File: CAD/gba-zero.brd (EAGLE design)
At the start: 130.7 x 72.9 mm, 55 parts, among them IC5 APX803, Q2 BSS138, U1 NC7WZ16, U4 LM4875

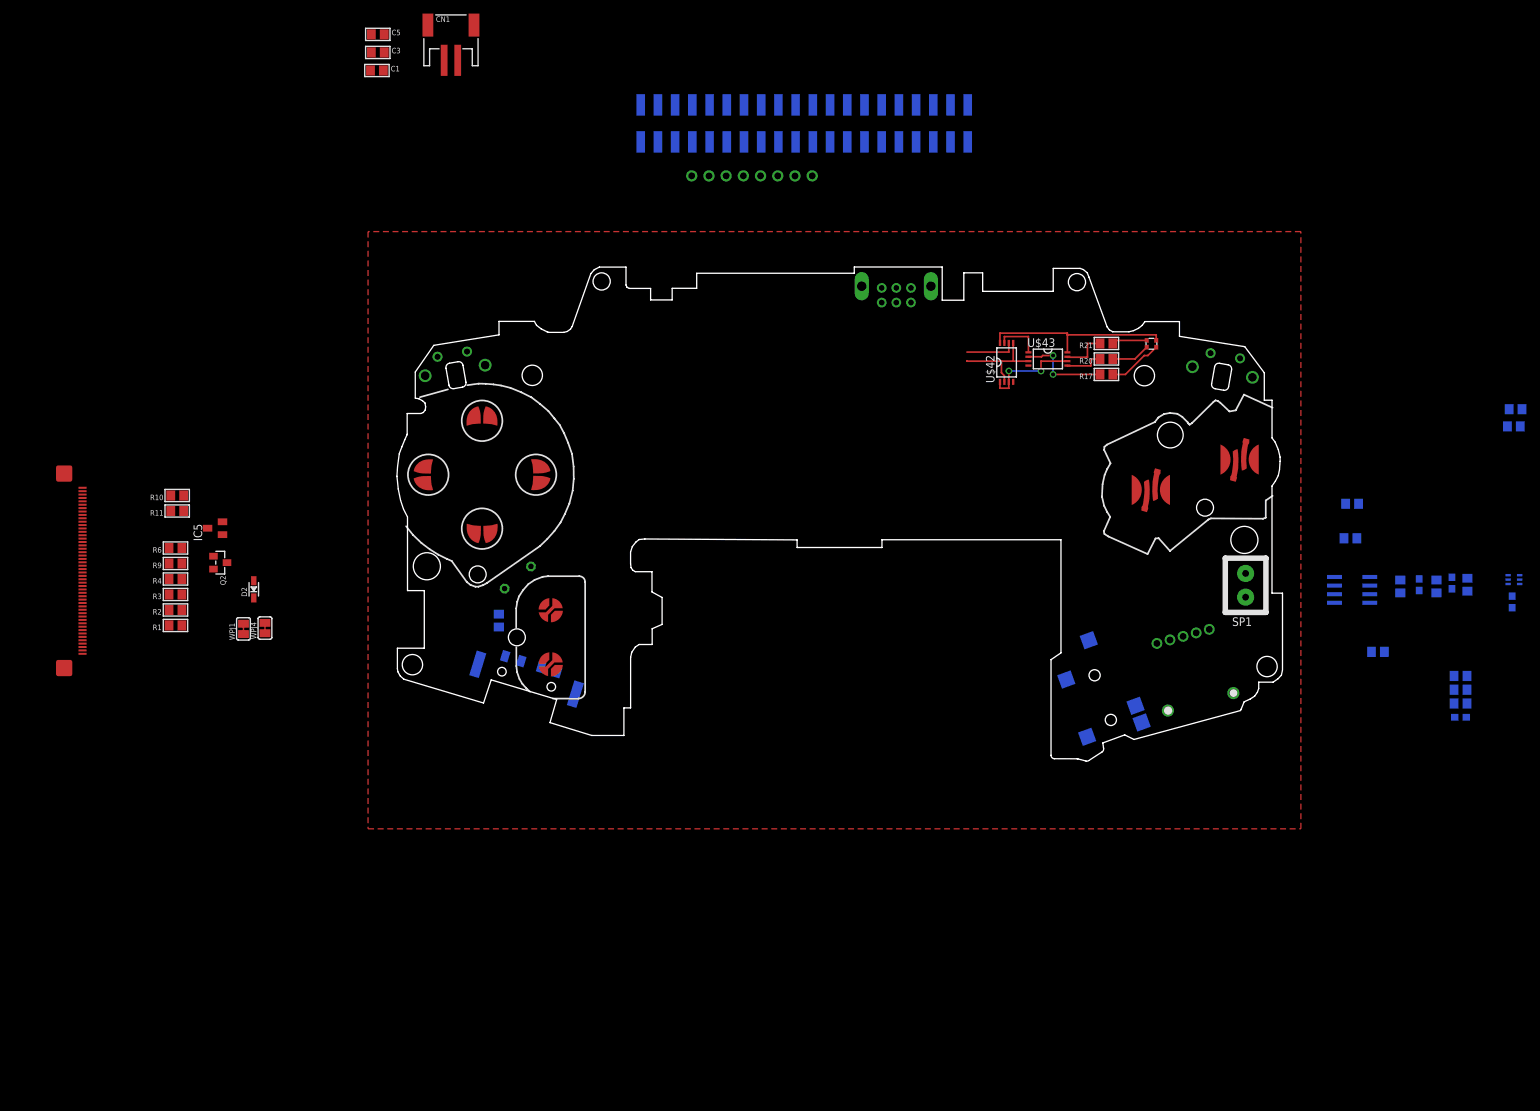
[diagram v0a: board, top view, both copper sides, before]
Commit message: Routed right side of the board
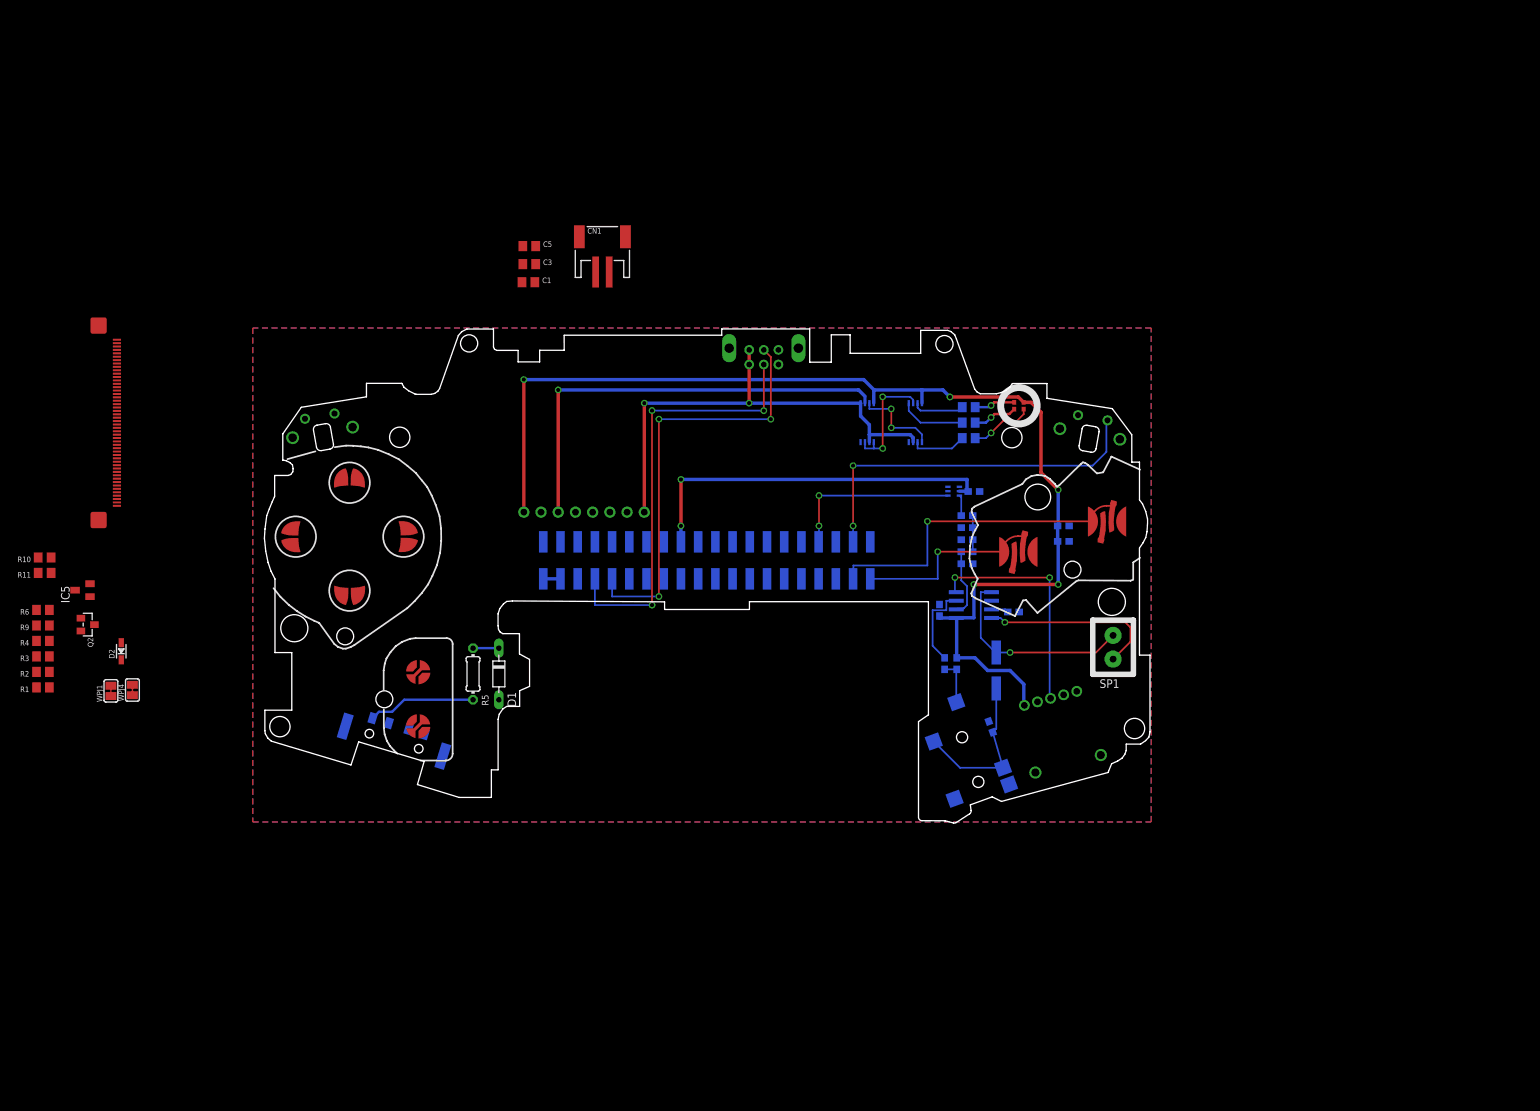
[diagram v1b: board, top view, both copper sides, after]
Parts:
- removed C15, C18: 10u, rcl:C0805
- removed C17: 100n, rcl:C0805
- removed C4: 100μF, rcl:C0603
- removed C8: 0.1μF, rcl:C0603
- removed R22, R23: 100K, microbuilder:0805
- removed U4: LM4875, texas:SOIC8
- added C10: 47μF, microbuilder:0603
- added C11: 10μF, microbuilder:0603
- added C7, C9: 0.1μF, microbuilder:0603
- added R13, R14: 100K, microbuilder:0603
- added U2: LM4875, gba-zero-parts:SO-8
- C12: value 10u -> 10μF; device rcl:C0805 -> microbuilder:0603
- C13: value 10u -> 100uF; device rcl:C0805 -> microbuilder:PANASONIC_D
- C2: value 0.1μF -> 1.0μF; device rcl:C0603 -> microbuilder:0603
- C6: value 47μF -> 1.0μF; device rcl:C0603 -> microbuilder:0603
- D1: device diode:D-5 -> diode:D-7.5
- R12, R24, R7, R8: device microbuilder:0805 -> microbuilder:0603
- R5: device microbuilder:0805 -> resistor:0204/7
- moved U1 83.7 mm to (103.4, 48.8), turned to 180 degrees
- moved R7 74.6 mm to (105.4, 45.2), turned to 0 degrees
- moved C6 70.9 mm to (101.3, 31.2)
- moved R8 69.6 mm to (105.4, 41.7), turned to 0 degrees
- moved R24 69.4 mm to (108.9, 14.0), turned to 250 degrees
- moved U$7 66.1 mm to (67.0, 38.6)
- moved C2 64.8 mm to (112.3, 31.0), turned to 180 degrees
- moved R12 64.0 mm to (105.4, 38.1), turned to 180 degrees
- moved C13 58.0 mm to (109.7, 22.4), turned to 90 degrees
- moved U$12 55.5 mm to (70.6, 44.5)
- moved C12 49.2 mm to (119.6, 41.4)
- moved C1 38.4 mm to (40.7, 79.7)
- moved C3 38.4 mm to (40.8, 82.3)
- moved CN1 38.4 mm to (51.6, 84.9)
- moved C5 38.4 mm to (40.8, 85.0)
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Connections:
- net N$19 renamed BAT
- removed net N$23: R22.1, U4.3
- removed net N$26: U$17.2, U4.4
- removed net N$30: C6.1, R12.1, U4.2
- removed net N$35: C12.1, U4.7
- removed net N$36: C4.1, SP1.1, U4.5
- removed net N$37: SP1.2, U4.8
- new net BYPASS: C2.1, U2.7
- new net IN-: C10.2, R12.1, U2.2
- new net SENSE: R14.2, U2.3
- new net VO1: C13.+, SP1.1, U2.5
- new net VO2: SP1.2, U2.8
- new net VOL/SD: U$17.2, U2.4
- net +5V: now also C11.2, C12.2, C6.2, R13.1, U2.1; no longer C13.2, C15.1, C17.1, C18.1, R23.1, U4.1
- net 3.3V: now also C7.1; no longer C8.2
- net BTN_A: now also U$7.38; no longer U$7.16
- net BTN_B: now also U$7.40; no longer U$7.32
- net BTN_D: now also U$7.15; no longer U$7.31
- net BTN_LS: now also L.SW; no longer L.BIG-1, L.SMALL-1
- net BTN_R: now also U$7.27; no longer U$7.15
- net BTN_RS: now also R.SW, U$7.37; no longer R.BIG-1, R.SMALL-1, U$7.11
- net BTN_SEL: now also U$7.32; no longer U$7.35
- net BTN_STR: now also U$7.28; no longer U$7.37
- net BTN_U: now also U$7.11; no longer U$7.29
- net GND: now also C11.1, C12.1, C2.2, C6.1, C7.2, C9.2, L.GND@1, L.GND@2, L.GND@3, R.GND@1, R.GND@2, R.GND@3, U2.6; no longer C12.2, C13.1, C15.2, C17.2, C18.2, C2.1, C8.1, L.BIG-2, L.SMALL-2, R.BIG-2, R.SMALL-2, U4.6
- net N$21: now also C10.1, C9.1; no longer C2.2, C6.2
- net N$22: now also R13.2, R14.1; no longer R22.2, R23.2
- net PWR_EN_RPI: now also U$7.16; no longer U$7.40
- net PWR_SW_SEN: now also U$7.26; no longer U$7.38
- net RING: now also C13.-; no longer C4.2
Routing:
- net +5V: track 28.2 -> 175.4 mm, vias 0 -> 5
- net TXD: track 0.00 -> 64.3 mm, vias 0 -> 3
- net RXD: track 0.00 -> 62.8 mm, vias 0 -> 3
- net LBO: track 7.52 -> 64.7 mm, vias 0 -> 1
- net 3.3V: track 0.00 -> 54.7 mm, vias 0 -> 2
- net USB: track 15.1 -> 69.5 mm, vias 0 -> 2
- net BTN_RS: track 0.00 -> 54.2 mm, vias 0 -> 2
- net BTN_A: track 0.00 -> 47.8 mm, vias 0 -> 1
- net VOL/SD: track 0.00 -> 34.2 mm, vias 0 -> 2
- net VO1: track 0.00 -> 29.8 mm, vias 0 -> 1
- net BTN_B: track 0.00 -> 27.7 mm, vias 0 -> 1
- net VO2: track 0.00 -> 26.8 mm, vias 0 -> 1
- net AUD_PWM: track 0.00 -> 25.9 mm, vias 0 -> 2
- net RING: track 0.00 -> 24.0 mm
- net N$17: track 0.00 -> 15.9 mm
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- added copper zone on layer 16, net GND

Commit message: More Routing
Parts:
- added C14, C4: 10μF, microbuilder:0603
- added C8: 0.1μF, microbuilder:0603
- moved R9 123.8 mm to (75.7, -33.7)
- moved U$2 117.3 mm to (62.1, -22.1)
- moved R6 117.1 mm to (70.3, -27.5), turned to 0 degrees
- moved Q2 116.6 mm to (75.7, -30.9), turned to 90 degrees
- moved R10 115.9 mm to (71.1, -16.3)
- moved R4 115.9 mm to (70.4, -29.4)
- moved R11 115.8 mm to (71.1, -18.4)
- moved R3 115.7 mm to (70.4, -31.5)
- moved R2 115.6 mm to (70.4, -33.5)
- moved R1 115.5 mm to (70.4, -35.5)
- moved IC5 110.9 mm to (70.1, -22.8), turned to 270 degrees
- moved D2 108.2 mm to (75.5, -26.7), turned to 270 degrees
- moved WPJ1 105.5 mm to (76.2, -21.9), turned to 180 degrees
- moved WPJ4 101.0 mm to (76.0, -18.0), turned to 180 degrees
- moved C1 56.6 mm to (-12.7, 60.9)
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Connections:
- net +5V: now also C14.1
- net 3.3V: now also C4.1, C8.1
- net GND: now also C14.2, C4.2, C8.2
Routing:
- net BTN_R: track 0.00 -> 80.8 mm, vias 0 -> 3
- net BTN_L: track 0.00 -> 77.3 mm, vias 0 -> 3
- net BTN_D: track 0.00 -> 75.4 mm, vias 0 -> 3
- net BTN_U: track 0.00 -> 67.3 mm, vias 0 -> 3
- net BTN_LS: track 0.00 -> 58.7 mm, vias 0 -> 2
- net 3.3V: track 54.7 -> 83.2 mm
- net N$1: track 0.00 -> 16.0 mm
- net TFT_RST: track 0.00 -> 9.49 mm
- net +5V: track 175.4 -> 184.4 mm
- net N$9: track 0.00 -> 8.50 mm
- net N$6: track 0.00 -> 7.55 mm
- net N$7: track 0.00 -> 6.23 mm
- net N$2: track 0.00 -> 5.86 mm
- net MOSI: track 0.00 -> 5.61 mm
- net SCLK: track 0.00 -> 5.41 mm
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
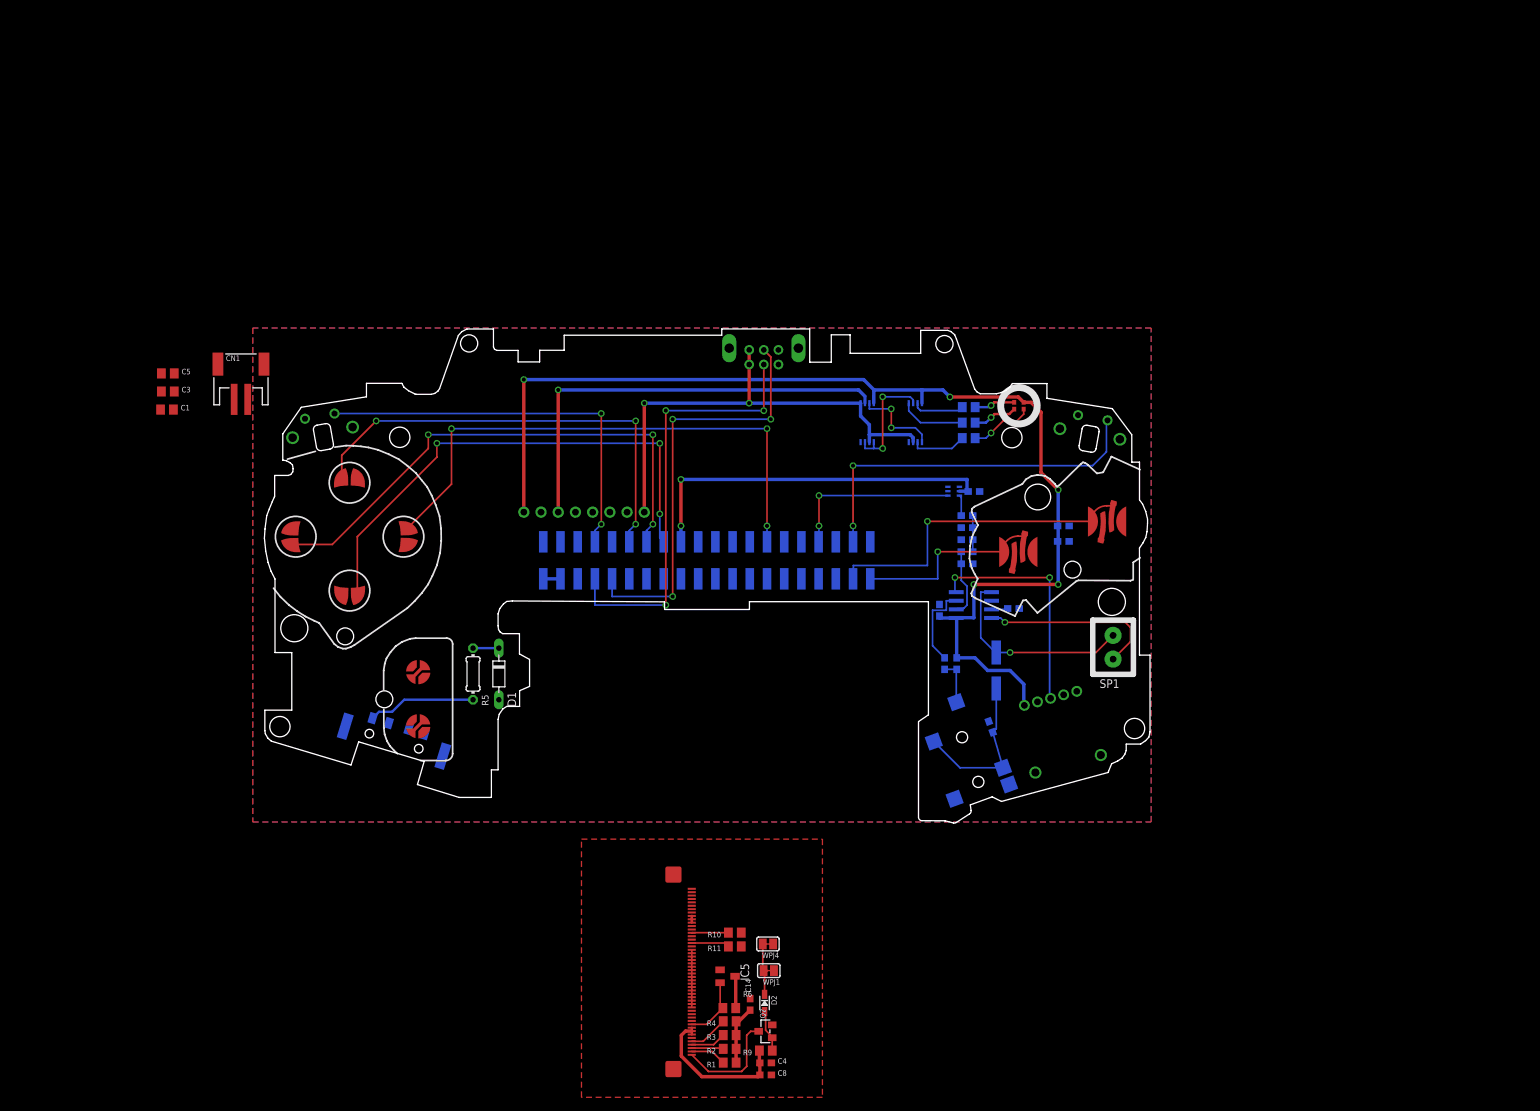
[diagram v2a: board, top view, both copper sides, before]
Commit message: Display is routed, some other stuff was unrouted
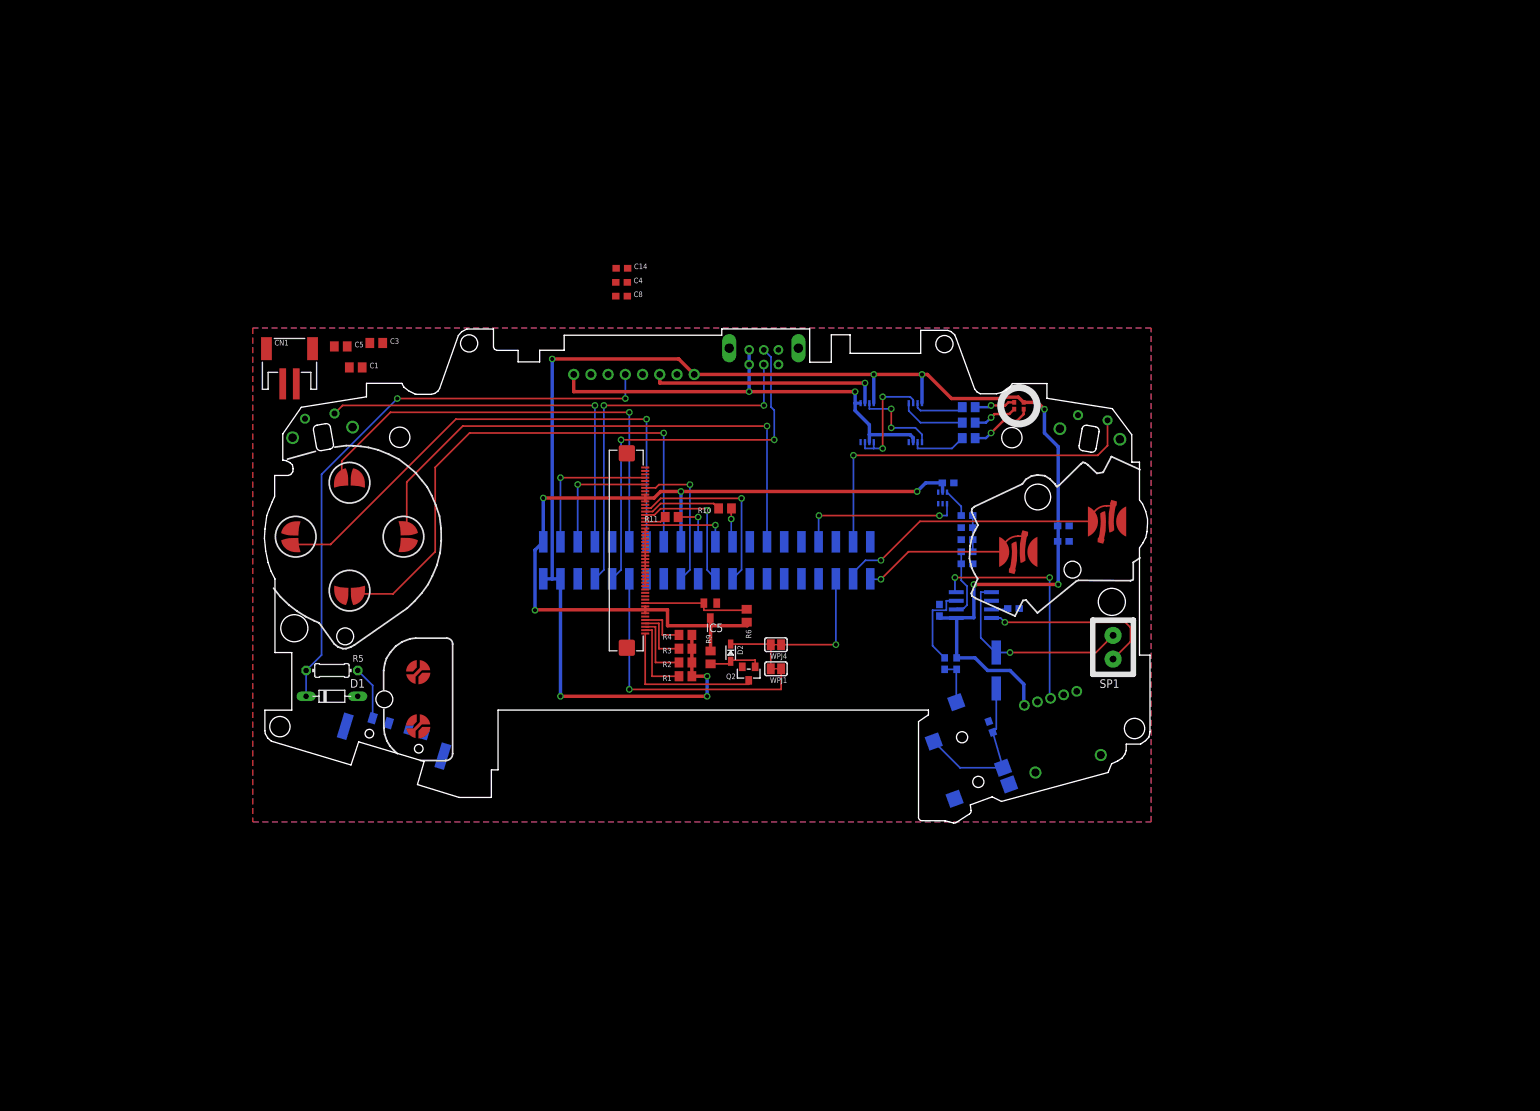
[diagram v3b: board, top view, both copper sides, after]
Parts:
- moved C4 117.1 mm to (54.4, 79.6)
- moved C8 116.9 mm to (54.4, 77.6)
- moved C14 110.3 mm to (54.5, 81.7), turned to 0 degrees
- moved R11 64.1 mm to (61.8, 45.0)
- moved R10 62.6 mm to (69.7, 46.3)
- moved U$2 62.6 mm to (55.3, 40.1)
- moved R9 58.6 mm to (67.6, 24.3), turned to 90 degrees
- moved R6 58.0 mm to (72.9, 30.4), turned to 270 degrees
- moved R1 57.4 mm to (63.9, 21.5)
- moved R2 57.4 mm to (63.9, 23.5)
- moved R3 57.4 mm to (63.9, 25.6)
- moved R4 57.4 mm to (63.9, 27.6)
- moved IC5 54.0 mm to (67.5, 31.2), turned to 180 degrees
- moved Q2 52.9 mm to (73.2, 21.9), turned to 180 degrees
- moved D2 51.9 mm to (70.5, 25.0)
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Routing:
- net N$18: track 3.81 -> 86.7 mm, vias 0 -> 2
- net +5V: track 184.4 -> 239.9 mm, vias 5 -> 9
- net 3.3V: track 83.2 -> 126.9 mm, vias 2 -> 4
- net BKLT_PWM: track 0.00 -> 41.8 mm, vias 0 -> 1
- net LBO: track 64.7 -> 34.5 mm
- net TFT_CS_3V: track 0.00 -> 27.2 mm, vias 0 -> 1
- net SDA: track 0.00 -> 22.0 mm, vias 0 -> 1
- net RT_INT: track 0.00 -> 21.2 mm, vias 0 -> 1
- net TFT_DC_3V: track 0.00 -> 20.2 mm, vias 0 -> 1
- net SCL: track 0.00 -> 18.4 mm, vias 0 -> 1
- net BKLT: track 0.00 -> 17.8 mm, vias 0 -> 1
- net MISO: track 0.00 -> 12.8 mm, vias 0 -> 1
- net TXD: track 64.3 -> 55.8 mm, vias 3 -> 2
- net N$17: track 15.9 -> 7.95 mm
- net N$1: track 16.0 -> 23.3 mm
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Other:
- outline, holes or cut-outs redrawn

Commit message: Fully Routed
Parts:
- moved C14 64.9 mm to (69.5, 18.5)
- moved C5 51.1 mm to (64.1, 68.5), flipped to the bottom
- moved C4 50.0 mm to (62.9, 30.3), turned to 90 degrees
- moved C8 48.4 mm to (64.9, 30.3), turned to 90 degrees
- moved C1 36.5 mm to (38.1, 38.6), flipped to the bottom
- moved C3 35.2 mm to (38.1, 41.7), flipped to the bottom
- moved CN1 31.1 mm to (26.9, 45.8), flipped to the bottom, turned to 180 degrees
- moved R5 1.52 mm to (11.7, 23.9), flipped to the bottom, turned to 180 degrees
- moved D1 0.25 mm to (11.7, 18.8), flipped to the bottom, turned to 180 degrees
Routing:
- net BTN_SEL: track 0.06 -> 73.4 mm, vias 0 -> 1
- net PWR_SW_SEN: track 0.06 -> 66.0 mm, vias 0 -> 2
- net BTN_STR: track 0.06 -> 64.4 mm, vias 0 -> 1
- net PWR_EN_RPI: track 0.00 -> 58.7 mm, vias 0 -> 1
- net BAT: track 0.00 -> 28.8 mm, vias 0 -> 2
- net 3.3V: track 126.9 -> 134.4 mm
- net +5V: track 239.9 -> 238.4 mm
- net N$17: track 7.95 -> 9.47 mm
- net BKLT_PWM: track 41.8 -> 40.8 mm
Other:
- outline, holes or cut-outs redrawn

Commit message: Cleared all DRC errors
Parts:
- removed WPJ1, WPJ4: 0, microbuilder:SOLDERJUMPER_CLOSEDWIRE
- added R15, R16: 0, microbuilder:0603
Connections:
- net BKLT: now also R15.2; no longer WPJ4.1
- net BKLT_PWM: now also R16.2; no longer WPJ1.1
- net N$6: now also R15.1, R16.1; no longer WPJ1.2, WPJ4.2
